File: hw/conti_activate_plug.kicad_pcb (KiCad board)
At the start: 2 copper layers, 38.2 x 45.5 mm, 38 parts, among them J1 Conn_01x02_Pin, J2 Conn_01x02_Pin, J3 Conn_01x02_Pin, J4 Conn_01x02_Pin, J5 Conn_01x02_Pin, J6 Conn_01x02_Pin, J7 Conn_01x02_Socket, Q1 BSS138, Q2 MMBTA06, Q3 BSS138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

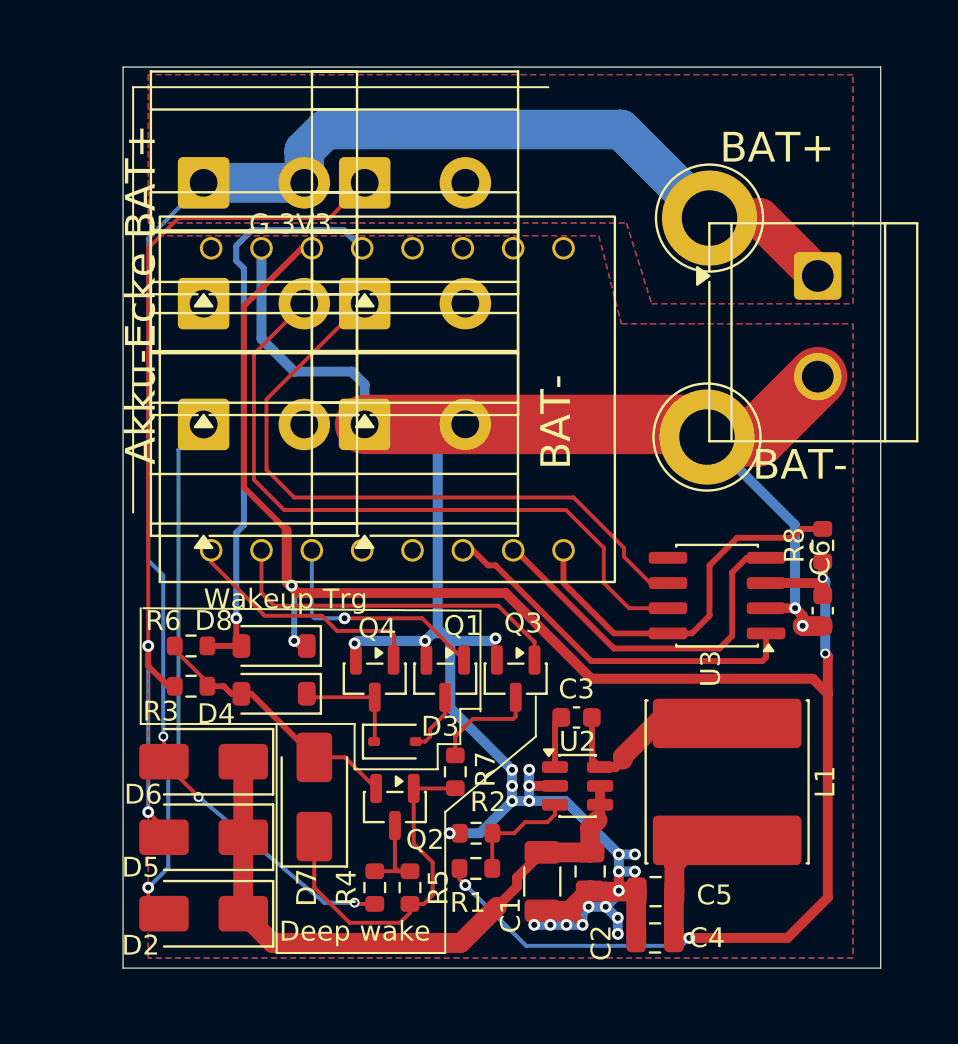
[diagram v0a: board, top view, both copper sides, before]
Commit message: Vext, CAN Terminierung, Mounting-Hole
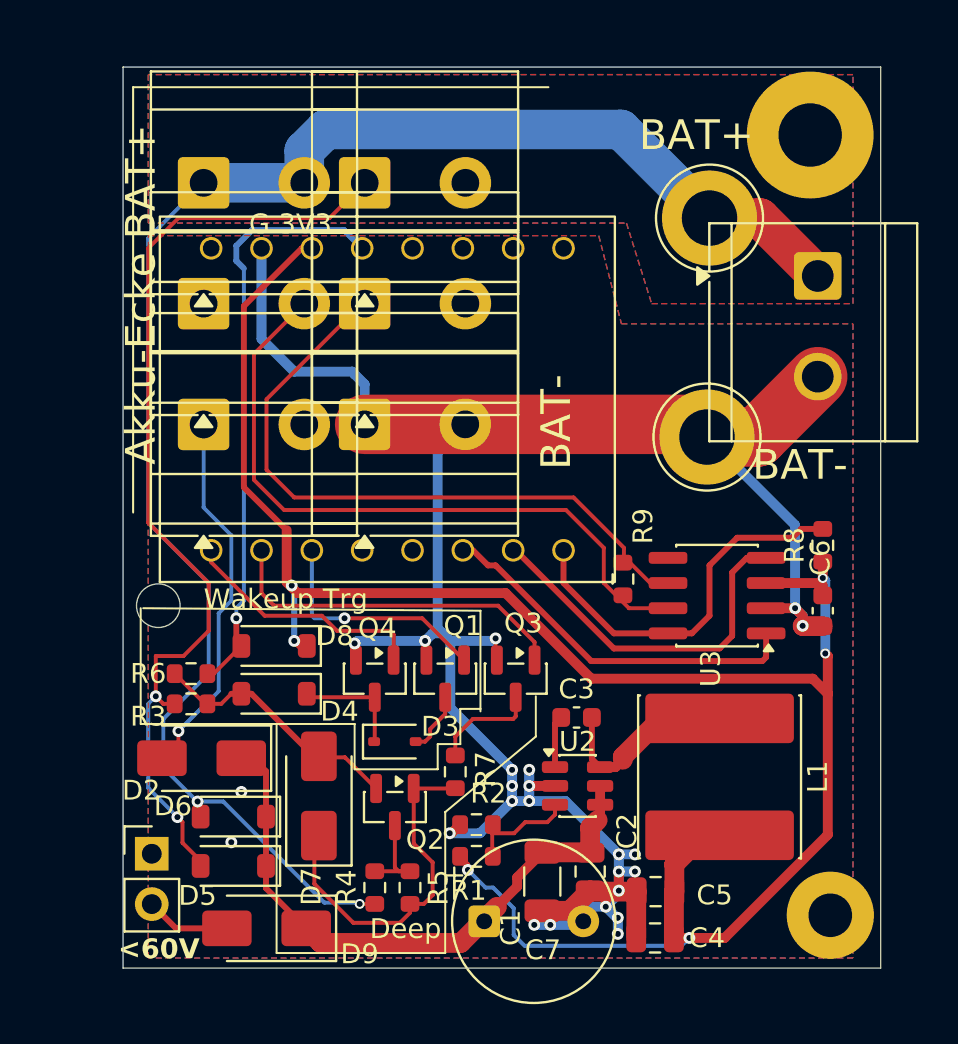
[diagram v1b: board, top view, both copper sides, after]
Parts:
- added C7: 100µF, Capacitor_THT:CP_Radial_Tantal_D8.0mm_P5.00mm, F.Cu at (103.8, 141.9)
- added D9: S1A, Diode_SMD:D_SMA, F.Cu at (92.8, 142.3)
- added J8: Vext, Connector_PinHeader_2.54mm:PinHeader_1x02_P2.54mm_Vertical, F.Cu at (87.0, 138.5)
- added R9: 120, Resistor_SMD:R_0603_1608Metric, F.Cu at (110.8, 124.6)
- added REF**: MountingHole_2.2mm_M2, MountingHole:MountingHole_2.2mm_M2, F.Cu at (87.4, 126.0)
- added REF**: MountingHole_2.2mm_M2_Pad, MountingHole:MountingHole_2.2mm_M2_Pad, F.Cu at (121.3, 141.6)
- added REF**: MountingHole_3.2mm_M3_Pad, MountingHole:MountingHole_3.2mm_M3_Pad, F.Cu at (120.3, 102.2)
- D5, D6: value S1A -> 1N4148W; footprint Diode_SMD:D_SMA -> Diode_SMD:D_SOD-123
- moved D2 7.85 mm to (89.6, 133.7)
- moved D6 3.15 mm to (91.2, 136.6)
- moved D5 2.08 mm to (91.2, 139.1)
- moved R6 1.40 mm to (89.0, 129.4)
- moved R3 0.89 mm to (89.0, 130.9)
- moved R1 0.61 mm to (103.4, 138.6)
- moved L1 0.46 mm to (115.7, 134.6)
- moved R2 0.43 mm to (103.4, 137.0)
- moved D7 0.23 mm to (95.5, 135.6)
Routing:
- net /12Vout: track 26.2 -> 18.9 mm
- net Net-(D9-A): track 0.00 -> 4.30 mm
- net /WAKEUP_VBAT+: track 45.1 -> 49.0 mm
- net /BAT+: track 80.2 -> 83.3 mm, vias 3 -> 2
- net GND: track 116.8 -> 119.2 mm, vias 25 -> 24
- net +3V3: track 102.8 -> 101.8 mm
- net Net-(D2-K): track 31.5 -> 32.3 mm
- net Net-(U2-FB): track 5.88 -> 5.28 mm
- net /WAKEUP_DETECT: track 29.4 -> 30.0 mm
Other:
- board text added: "<60V"
- board text added: "Deep"
- board text added: "Diese Seite zeigt zum Akku"
- board text removed: "Deep wake"

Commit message: Stepdown redesigned, TCAN3414, S1B
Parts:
- removed D2, D7: S1A, Diode_SMD:D_SMA
- removed D4, D5, D6, D8: 1N4148W, Diode_SMD:D_SOD-123
- removed REF**: MountingHole_2.2mm_M2, MountingHole:MountingHole_2.2mm_M2
- removed REF**: MountingHole_2.2mm_M2_Pad, MountingHole:MountingHole_2.2mm_M2_Pad
- removed REF**: MountingHole_3.2mm_M3_Pad, MountingHole:MountingHole_3.2mm_M3_Pad
- added D10: S1B, Diode_SMD:D_SOD-123F, F.Cu at (92.5, 137.2)
- added D11: S1B, Diode_SMD:D_SOD-123F, F.Cu at (90.6, 133.8)
- added D12: S1B, Diode_SMD:D_SOD-123F, F.Cu at (92.5, 139.6)
- added D13: S1B, Diode_SMD:D_SOD-123F, F.Cu at (93.4, 128.3)
- added D14: S1B, Diode_SMD:D_SOD-123F, F.Cu at (93.4, 130.9)
- added D15: S1B, Diode_SMD:D_SOD-123F, F.Cu at (96.0, 134.4)
- added H1: MountingHole, MountingHole:MountingHole_3.2mm_M3, F.Cu at (120.4, 102.2)
- added H2: MountingHole, MountingHole:MountingHole_3.2mm_M3, F.Cu at (106.3, 135.4)
- added H3: MountingHole, MountingHole:MountingHole_2.2mm_M2, F.Cu at (87.5, 126.4)
- added J9: Conn_01x01_Socket, Connector_PinHeader_2.54mm:PinHeader_1x01_P2.54mm_Vertical, F.Cu at (87.3, 135.8)
- added R10: 32k, Resistor_SMD:R_0603_1608Metric, F.Cu at (115.1, 120.7)
- C2: footprint Capacitor_SMD:C_0805_2012Metric -> Capacitor_SMD:C_0603_1608Metric
- C7: value 100µF -> 470µF
- D9: value S1A -> S1B; footprint Diode_SMD:D_SMA -> Diode_SMD:D_SOD-123F
- J1, J2, J3, J4, J5, J6: footprint TerminalBlock_MetzConnect:TerminalBlock_MetzConnect_Type073_RT02602HBLU_1x02_P5.08mm_Horizontal -> Library:1x02_P5.08mm
- Q1, Q3, Q4: value BSS138 -> BSS123L
- R8: value 100k -> 32k
- U3: value SN65HVD230 -> SN65HVD230 // tcan3414
- moved C1 11.2 mm to (117.9, 141.2)
- moved C4 7.50 mm to (112.8, 135.3), turned to -90 degrees
- moved C3 7.22 mm to (112.0, 137.9)
- moved U2 6.95 mm to (112.0, 141.1)
- moved C2 6.86 mm to (115.6, 141.9)
- moved R2 6.47 mm to (108.5, 141.1), turned to 90 degrees
- moved C5 5.44 mm to (110.7, 135.3), turned to -90 degrees
- moved R8 4.44 mm to (117.1, 120.7), turned to -90 degrees
- moved R1 4.28 mm to (106.9, 141.1), turned to -90 degrees
- moved L1 2.43 mm to (118.1, 134.4), turned to 90 degrees
- moved TP2 2.39 mm to (114.0, 115.3)
- moved TP1 1.90 mm to (114.0, 108.0)
- moved C7 1.58 mm to (102.6, 142.9), turned to 90 degrees
- moved D9 0.38 mm to (92.5, 142.2)
- moved J8 0.28 mm to (87.2, 138.3)
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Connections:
- net /CAN_STBY renamed /~{CAN_STBY}
- U1 pad 4: unconnected-(U1-GPIO3-Pad4) -> /CAN_SHUTDOWN
- U3 pad 5: unconnected-(U3-Vref-Pad5) -> /CAN_SHUTDOWN
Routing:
- net /CAN_SHUTDOWN: track 0.00 -> 41.1 mm
- net GND: track 119.2 -> 92.3 mm, vias 24 -> 17
- net Net-(D10-K): track 32.3 -> 45.9 mm, vias 0 -> 1
- net +3V3: track 101.8 -> 91.5 mm, vias 6 -> 2
- net /~{CAN_STBY}: track 19.5 -> 16.2 mm
- net /BAT+: track 83.3 -> 85.1 mm, vias 2 -> 3
- net Net-(U2-SW): track 10.5 -> 12.1 mm
- net Net-(D15-K): track 17.9 -> 19.4 mm
- net /WAKEUP_VBAT+: track 49.0 -> 50.4 mm
- net Net-(U2-FB): track 5.28 -> 3.99 mm
- net /WAKEUP_DETECT: track 30.0 -> 30.7 mm
- added copper zone on F.Cu, net +3V3
- added copper zone on F.Cu, net Net-(D10-K)
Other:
- board text added: "+<60V"
- board text added: "12V"
- board text added: "22-33µH"
- board text added: "Akku-Ecke"
- board text added: "ESP32C3 Super Mini"
- board text added: "Flachstecker andere Seite!"
- board text added: "GND"
- board text added: "LMR51610X"
- board text added: "POWER"
- board text added: "TCAN3414 65HVD230"
- board text added: "VEXT"
- board text added: "WK"
- board text added: "WKUP"
- board text added: "https://github.com/NerdyProjects/conti_bat_trigger 2026 by Matthias Larisch"
- board text added: "v1 2026-04-21"
- board text removed: "<60V"
- board text removed: "https://github.com/NerdyProjects/conti_bat_trigger 2026 by Matthias Larisch v1 2026-04-21"

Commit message: forgot hw/sch
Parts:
- removed D14, D15: S1B, Diode_SMD:D_SOD-123F
- removed R4: 10k, Resistor_SMD:R_0603_1608Metric
- removed R5: 1M, Resistor_SMD:R_0603_1608Metric
- removed R7: 100k, Resistor_SMD:R_0603_1608Metric
- added C8: 100n 100V, Capacitor_SMD:C_0603_1608Metric, F.Cu at (95.0, 131.3)
- added JP1: Jumper_2_Bridged, Jumper:SolderJumper-2_P1.3mm_Bridged_RoundedPad1.0x1.5mm, F.Cu at (111.5, 130.6)
- added JP2: Jumper_2_Open, Jumper:SolderJumper-2_P1.3mm_Open_RoundedPad1.0x1.5mm, F.Cu at (107.4, 130.3)
- added R11: 470k, Resistor_SMD:R_0603_1608Metric, F.Cu at (93.5, 128.5)
- added R12: 33k, Resistor_SMD:R_0603_1608Metric, F.Cu at (95.0, 128.5)
- added R13: 100k, Resistor_SMD:R_0603_1608Metric, F.Cu at (102.4, 136.3)
- added R14: 1M, Resistor_SMD:R_0603_1608Metric, F.Cu at (106.7, 136.0)
- added R15: 2R2, Resistor_SMD:R_0603_1608Metric, F.Cu at (96.8, 141.5)
- C4, C5: value 10µF 10V -> 10µF 16V
- D3: footprint Diode_SMD:D_SOD-323 -> Diode_SMD:D_SOD-123F
- H3: footprint MountingHole:MountingHole_2.2mm_M2 -> MountingHole:MountingHole_3.2mm_M3
- Q2: value MMBTA06 -> BSS123L
- Q3: value BSS123L -> BSS83P
- R10, R2, R8: value 32k -> 33k
- R6: value 470k -> 1M
- moved H3 36.8 mm to (121.0, 141.7)
- moved H2 19.9 mm to (87.7, 128.4)
- moved Q3 10.1 mm to (102.4, 139.3)
- moved D13 8.02 mm to (97.4, 135.3)
- moved Q2 5.29 mm to (103.9, 133.5), turned to 0 degrees
- moved C7 3.38 mm to (99.2, 142.7)
- moved R6 3.05 mm to (91.9, 128.5), turned to -90 degrees
- moved R3 2.95 mm to (91.9, 131.3)
- moved C1 1.27 mm to (116.6, 141.2)
- moved C2 0.89 mm to (114.7, 141.9)
- moved U2 0.65 mm to (111.4, 141.0)
- moved R1 0.51 mm to (106.4, 141.1)
- moved R2 0.51 mm to (108.0, 141.1)
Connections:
- C1 pad 1: Net-(D10-K) -> Net-(U2-EN)
- C2 pad 1: Net-(D10-K) -> Net-(U2-EN)
- C4 pad 1: +3V3 -> +5V
- C5 pad 1: +3V3 -> +5V
- C7 pad 1: Net-(D10-K) -> Net-(U2-EN)
- D13 pad 1: +3V3 -> Net-(D13-K)
- D13 pad 2: /WAKEUP_DETECT -> /BAT+
- D3 pad 1: Net-(D14-K) -> Net-(D3-K)
- L1 pad 2: +3V3 -> +5V
- Q2 pad 1: Net-(D15-K) -> /WAKEUP_PU
- Q2 pad 2: Net-(D14-A) -> GND
- Q3 pad 1: /WAKEUP_INH_PULLUP -> Net-(Q3-G)
- Q3 pad 2: GND -> Net-(D13-K)
- Q3 pad 3: Net-(Q3-D) -> Net-(D3-K)
- Q4 pad 3: Net-(D14-K) -> Net-(D3-K)
- R1 pad 1: +3V3 -> +5V
- R3 pad 2: Net-(D14-A) -> Net-(D3-K)
- R6 pad 2: Net-(D14-A) -> Net-(D3-K)
- U1 pad 10: /WAKEUP_INH_PULLUP -> /WAKEUP_PU
- U1 pad 8: unconnected-(U1-5V-Pad8) -> Net-(JP2-B)
- U2 pad 4: Net-(D10-K) -> Net-(U2-EN)
- U2 pad 5: Net-(D10-K) -> Net-(U2-EN)
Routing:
- net Net-(JP2-B): track 0.00 -> 35.6 mm, vias 0 -> 1
- net Net-(D10-K): track 45.9 -> 11.9 mm, vias 1 -> 0
- net Net-(U2-EN): track 0.00 -> 29.7 mm, vias 0 -> 1
- net +3V3: track 91.5 -> 66.2 mm, vias 2 -> 0
- net Net-(D3-K): track 0.00 -> 25.0 mm
- net +5V: track 0.00 -> 24.1 mm
- net Net-(D15-K): track 19.4 -> 0.00 mm
- net /WAKEUP_INH_PULLUP: track 17.9 -> 0.00 mm
- net /WAKEUP_PU: track 0.00 -> 17.7 mm, vias 0 -> 1
- net Net-(D14-A): track 13.0 -> 0.00 mm
- net Net-(D14-K): track 6.31 -> 0.00 mm
- net Net-(Q3-G): track 0.00 -> 5.89 mm
- net Net-(Q3-D): track 5.39 -> 0.00 mm
- net Net-(D13-K): track 0.00 -> 5.31 mm
- net /BAT+: track 85.1 -> 80.5 mm
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- added copper zone on F.Cu, net +5V
- added copper zone on F.Cu, net Net-(U2-EN)
- added copper zone on F.Cu, net Net-(U2-SW)
- removed copper zone on F.Cu, net +3V3
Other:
- board text added: "+<50V"
- board text added: "5V G 3V3"
- board text added: "BAT+ WAKEUP"
- board text added: "Buck3,3V"
- board text added: "ESP5V"
- board text added: "JP1: Buck 3,3V Vcc JP2: Buck ESP32 5Vin (Feedback R2 auf 20k!)"
- board text removed: "+<60V"
- board text removed: "Akku-Ecke BAT+"
- board text removed: "BAT+ WAKEUP_VBAT"
- board text removed: "G 3V3"

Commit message: v2
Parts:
- added R16: 100k, Resistor_SMD:R_0603_1608Metric, F.Cu at (98.3, 127.1)
- added R17: 33k, Resistor_SMD:R_0603_1608Metric, F.Cu at (109.1, 111.6)
- added R18: 1M, Resistor_SMD:R_0603_1608Metric, F.Cu at (109.1, 109.7)
- added R19: 100k, Resistor_SMD:R_0603_1608Metric, F.Cu at (111.9, 143.0)
- added R20: 470k, Resistor_SMD:R_0603_1608Metric, F.Cu at (108.8, 143.0)
- added R4: 33k, Resistor_SMD:R_0603_1608Metric, F.Cu at (98.8, 140.2)
- added R5: 100k, Resistor_SMD:R_0603_1608Metric, F.Cu at (102.4, 133.6)
- added R7: 100k, Resistor_SMD:R_0603_1608Metric, F.Cu at (101.8, 126.9)
- C4, C5: value 10µF 16V -> 22µF 25V
- R9: value 120 -> 200
- moved Q2 1.28 mm to (105.2, 133.6)
- moved R1 0.75 mm to (106.7, 140.4)
- moved R2 0.75 mm to (108.2, 140.4)
- moved C2 0.59 mm to (114.5, 141.3)
- moved U2 0.47 mm to (111.4, 140.5)
- moved R14 0.26 mm to (106.9, 136.0)
- moved J2 0.12 mm to (97.9, 116.8)
- moved J4 0.11 mm to (97.9, 110.7)
- moved J5 0.11 mm to (97.9, 104.6)
- moved Q4 0.10 mm to (98.3, 129.8)
- moved U1 0.08 mm to (98.9, 115.7)
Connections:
- C1 pad 1: Net-(U2-EN) -> Net-(U2-VIN)
- C2 pad 1: Net-(U2-EN) -> Net-(U2-VIN)
- C7 pad 1: Net-(U2-EN) -> Net-(U2-VIN)
- Q3 pad 3: Net-(D3-K) -> Net-(Q3-D)
- R15 pad 1: Net-(U2-EN) -> Net-(U2-VIN)
- U1 pad 1: unconnected-(U1-GPIO0-Pad1) -> Net-(U1-GPIO0)
- U2 pad 5: Net-(U2-EN) -> Net-(U2-VIN)
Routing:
- net Net-(U2-VIN): track 0.00 -> 29.8 mm, vias 0 -> 2
- net Net-(U2-EN): track 29.7 -> 3.60 mm, vias 1 -> 0
- net /BAT+: track 80.5 -> 85.3 mm
- net Net-(U1-GPIO0): track 0.00 -> 4.09 mm
- net Net-(D3-K): track 25.0 -> 21.2 mm
- net GND: track 94.0 -> 97.6 mm, vias 24 -> 25
- net Net-(U2-SW): track 12.4 -> 9.16 mm
- net Net-(Q3-D): track 0.00 -> 2.82 mm
- net /WAKEUP_PU: track 17.7 -> 19.4 mm
- net /WAKEUP_PD_12: track 11.9 -> 13.3 mm
- net Net-(Q2-D): track 3.20 -> 1.96 mm
- net Net-(U2-CB): track 2.96 -> 2.04 mm
- net +5V: track 24.1 -> 23.5 mm
- net unconnected-(U1-GPIO1-Pad2): track 0.00 -> 0.58 mm
- added copper zone on F.Cu, net Net-(U2-VIN)
- removed copper zone on F.Cu, net Net-(D10-K)
- removed copper zone on F.Cu, net Net-(U2-EN)
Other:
- board text added: "v2 2026-05-29"
- board text removed: "LMR51610X"
- board text removed: "v1 2026-04-21"
